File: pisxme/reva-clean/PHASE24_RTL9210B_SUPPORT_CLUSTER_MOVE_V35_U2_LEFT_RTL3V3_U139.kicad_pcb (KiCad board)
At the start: 6 copper layers, 80 x 45 mm, 12 parts, among them J1 M.2 Socket 3 M-key 2280, U1 RTL9210B-CG, U2 W25Q128_SPI_FLASH, Y1 XTAL_25MHz

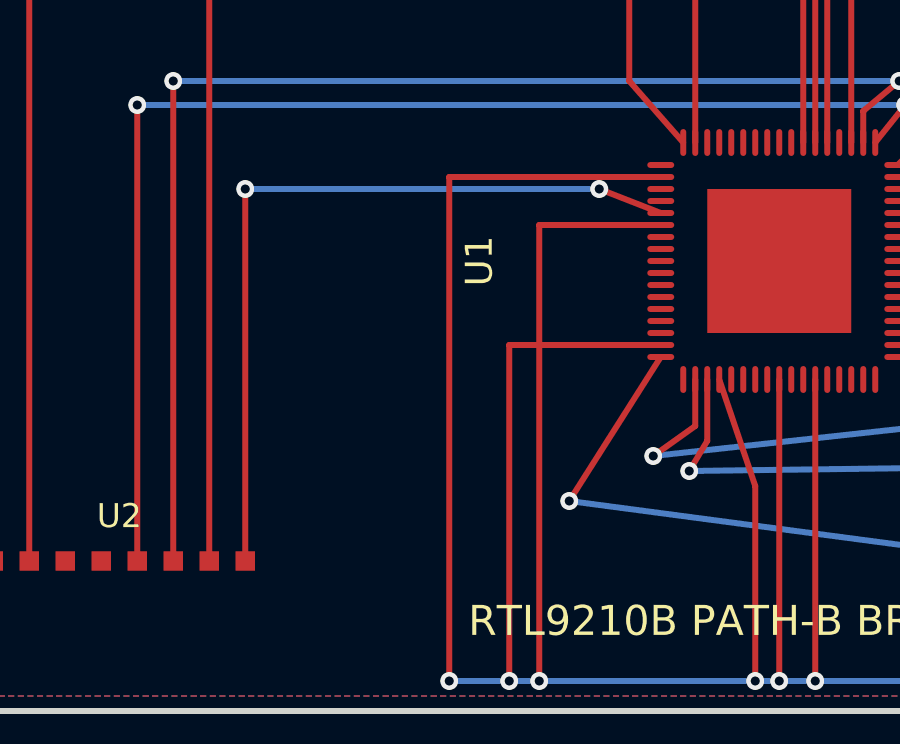
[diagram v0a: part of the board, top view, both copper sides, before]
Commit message: record RTL9210B shallow 3V3 escape rejection
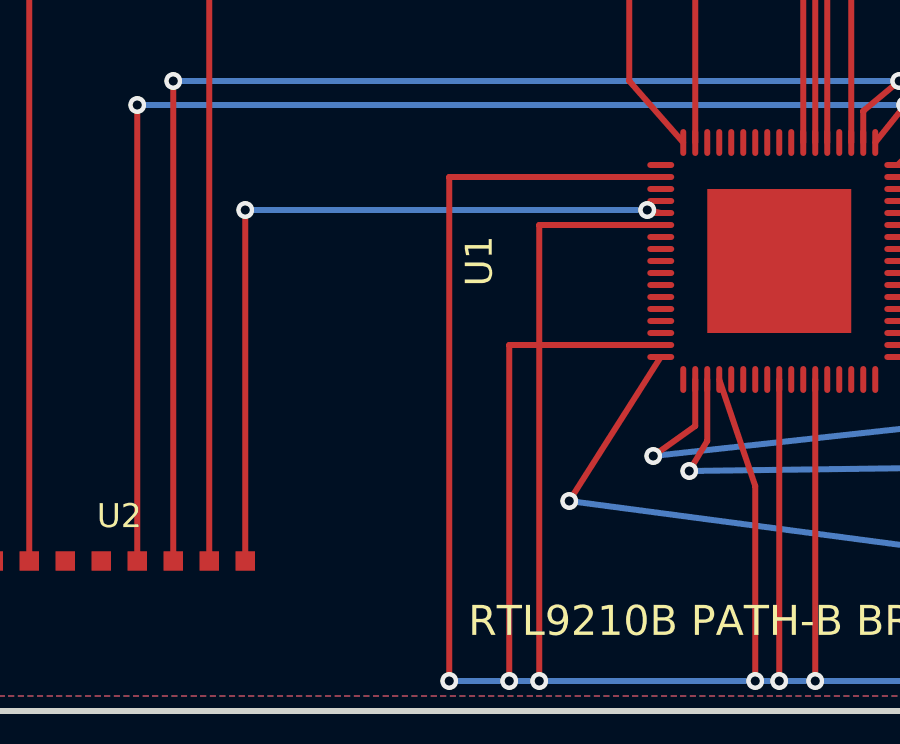
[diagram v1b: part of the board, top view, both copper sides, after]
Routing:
- net RTL_3V3: track 93.1 -> 92.3 mm
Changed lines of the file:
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@@
+	)
+	(segment
+		(start 89 72.8)
+		(end 89 84)
+		(width 0.2)
+		(layer "F.Cu")
+		(net "RTL_1V1")
+	)
+	(segment
+		(start 90 68.8)
+		(end 90 84)
+		(width 0.2)
+		(layer "F.Cu")
+		(net "RTL_1V1")
+	)
+	(segment
+		(start 94.05 72.8)
+		(end 89 72.8)
+		(width 0.2)
+		(layer "F.Cu")
+		(net "RTL_1V1")
+	)
+	(segment
+		(start 87 67.2)
+		(end 87 84)
+		(width 0.2)
+		(layer "F.Cu")
+		(net "RTL_1V1")
+	)
+	(segment
+		(start 94.05 68.8)
+		(end 90 68.8)
+		(width 0.2)
+		(layer "F.Cu")
+		(net "RTL_1V1")
+	)
+	(segment
+		(start 96 73.95)
+		(end 97.2 77.5)
+		(width 0.2)
+		(layer "F.Cu")
+		(net "RTL_1V1")
+	)
+	(segment
+		(start 94.05 67.2)
+		(end 87 67.2)
+		(width 0.2)
+		(layer "F.Cu")
+		(net "RTL_1V1")
+	)
+	(segment
+		(start 104 84)
+		(end 104 82)
+		(width 0.2)
+		(layer "F.Cu")
+		(net "RTL_1V1")
+	)
+	(segment
+		(start 98 73.95)
+		(end 98 84)
+		(width 0.2)
+		(layer "F.Cu")
+		(net "RTL_1V1")
+	)
+	(segment
+		(start 97.2 77.5)
+		(end 97.2 84)
+		(width 0.2)
+		(layer "F.Cu")
+		(net "RTL_1V1")
 	)
 	(segment
@@
 		(net "RTL_1V1")
 	)
-	(segment
-		(start 94.05 72.8)
-		(end 89 72.8)
-		(width 0.2)
-		(layer "F.Cu")
-		(net "RTL_1V1")
-	)
-	(segment
-		(start 98 73.95)
-		(end 98 84)
-		(width 0.2)
-		(layer "F.Cu")
-		(net "RTL_1V1")
-	)
-	(segment
-		(start 96 73.95)
-		(end 97.2 77.5)
-		(width 0.2)
-		(layer "F.Cu")
-		(net "RTL_1V1")
-	)
-	(segment
-		(start 87 67.2)
-		(end 87 84)
-		(width 0.2)
-		(layer "F.Cu")
-		(net "RTL_1V1")
-	)
-	(segment
-		(start 89 72.8)
-		(end 89 84)
-		(width 0.2)
-		(layer "F.Cu")
-		(net "RTL_1V1")
-	)
-	(segment
-		(start 94.05 68.8)
-		(end 90 68.8)
-		(width 0.2)
-		(layer "F.Cu")
-		(net "RTL_1V1")
-	)
-	(segment
-		(start 94.05 67.2)
-		(end 87 67.2)
-		(width 0.2)
-		(layer "F.Cu")
-		(net "RTL_1V1")
-	)
-	(segment
-		(start 90 68.8)
-		(end 90 84)
-		(width 0.2)
-		(layer "F.Cu")
-		(net "RTL_1V1")
-	)
-	(segment
-		(start 104 84)
-		(end 104 82)
-		(width 0.2)
-		(layer "F.Cu")
-		(net "RTL_1V1")
-	)
-	(segment
-		(start 97.2 77.5)
-		(end 97.2 84)
-		(width 0.2)
-		(layer "F.Cu")
+	(via
+		(at 104 84)
+		(size 0.6)
+		(drill 0.3)
+		(layers "F.Cu" "B.Cu")
+		(net "RTL_1V1")
+	)
+	(via
+		(at 98 84)
+		(size 0.6)
+		(drill 0.3)
+		(layers "F.Cu" "B.Cu")
+		(net "RTL_1V1")
+	)
+	(via
+		(at 87 84)
+		(size 0.6)
+		(drill 0.3)
+		(layers "F.Cu" "B.Cu")
+		(net "RTL_1V1")
+	)
+	(via
+		(at 89 84)
+		(size 0.6)
+		(drill 0.3)
+		(layers "F.Cu" "B.Cu")
+		(net "RTL_1V1")
+	)
+	(via
+		(at 99.2 84)
+		(size 0.6)
+		(drill 0.3)
+		(layers "F.Cu" "B.Cu")
+		(net "RTL_1V1")
+	)
+	(via
+		(at 90 84)
+		(size 0.6)
+		(drill 0.3)
+		(layers "F.Cu" "B.Cu")
 		(net "RTL_1V1")
 	)
 	(via
 		(at 97.2 84)
-		(size 0.6)
-		(drill 0.3)
-		(layers "F.Cu" "B.Cu")
-		(net "RTL_1V1")
-	)
-	(via
-		(at 89 84)
-		(size 0.6)
-		(drill 0.3)
-		(layers "F.Cu" "B.Cu")
-		(net "RTL_1V1")
-	)
-	(via
-		(at 104 84)
-		(size 0.6)
-		(drill 0.3)
-		(layers "F.Cu" "B.Cu")
-		(net "RTL_1V1")
-	)
-	(via
-		(at 99.2 84)
-		(size 0.6)
-		(drill 0.3)
-		(layers "F.Cu" "B.Cu")
-		(net "RTL_1V1")
-	)
-	(via
-		(at 87 84)
-		(size 0.6)
-		(drill 0.3)
-		(layers "F.Cu" "B.Cu")
-		(net "RTL_1V1")
-	)
-	(via
-		(at 90 84)
-		(size 0.6)
-		(drill 0.3)
-		(layers "F.Cu" "B.Cu")
-		(net "RTL_1V1")
-	)
-	(via
-		(at 98 84)
 		(size 0.6)
 		(drill 0.3)
@@
 	)
 	(segment
-		(start 80.2 67.6)
-		(end 80.2 80)
-		(width 0.2)
-		(layer "F.Cu")
-		(net "RTL_3V3")
-	)
-	(segment
 		(start 93 64)
 		(end 93 54)
@@
 	)
 	(segment
-		(start 94.05 68.4)
-		(end 92 67.6)
+		(start 80.2 68.3)
+		(end 80.2 80)
 		(width 0.2)
 		(layer "F.Cu")
@@
 	)
 	(segment
+		(start 94.05 68.4)
+		(end 93.6 68.3)
+		(width 0.2)
+		(layer "F.Cu")
+		(net "RTL_3V3")
+	)
+	(segment
 		(start 90.2 54)
 		(end 93 54)
@@
 	)
 	(via
-		(at 80.2 67.6)
-		(size 0.6)
-		(drill 0.3)
-		(layers "F.Cu" "B.Cu")
-		(net "RTL_3V3")
-	)
-	(via
 		(at 110 60.8)
 		(size 0.6)
@@
 	)
 	(via
-		(at 92 67.6)
+		(at 80.2 68.3)
+		(size 0.6)
+		(drill 0.3)
+		(layers "F.Cu" "B.Cu")
+		(net "RTL_3V3")
+	)
+	(via
+		(at 93.6 68.3)
 		(size 0.6)
 		(drill 0.3)
@@
 	)
 	(segment
-		(start 92 67.6)
-		(end 80.2 67.6)
-		(width 0.2)
-		(layer "B.Cu")
-		(net "RTL_3V3")
-	)
-	(segment
 		(start 110 60.8)
 		(end 110 68.5)
 		(width 0.2)
 		(layer "B.Cu")
+		(net "RTL_3V3")
+	)
+	(segment
+		(start 93.6 68.3)
+		(end 80.2 68.3)
+		(width 0.2)
+		(layer "B.Cu")
